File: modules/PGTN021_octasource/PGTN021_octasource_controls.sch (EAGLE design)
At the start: 81 parts

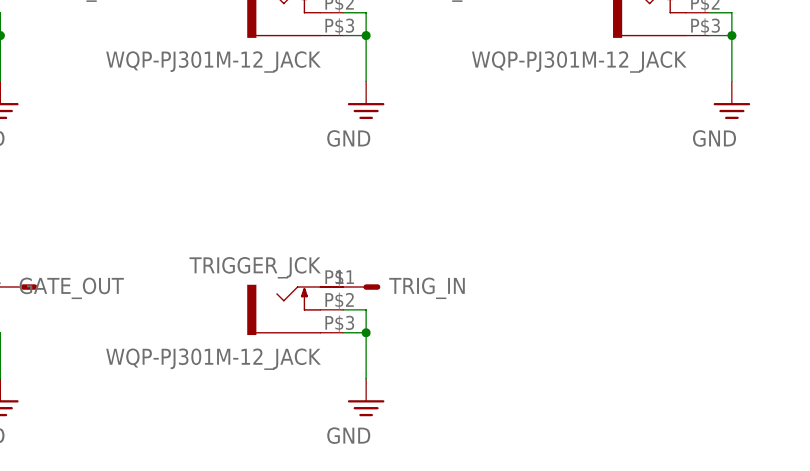
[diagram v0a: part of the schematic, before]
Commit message: Modified boards to fit together better
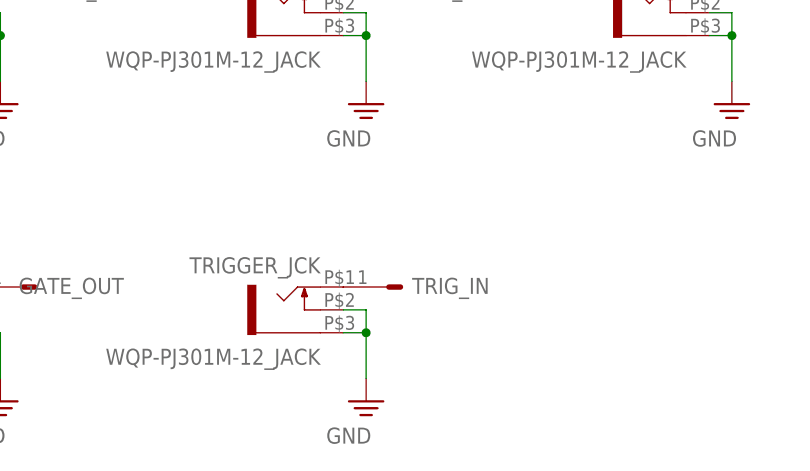
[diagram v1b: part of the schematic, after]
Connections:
- new net N$38: TRIGGER_JCK.2, TRIG_IN.3
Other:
- moved on the sheet: TRIG_IN
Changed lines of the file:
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@@
 <instance part="LENGTH_CV" gate="HEADER" x="45.72" y="-10.16" rot="R180"/>
 <instance part="GATE_OUT" gate="HEADER" x="-35.56" y="-43.18" rot="R180"/>
-<instance part="TRIG_IN" gate="HEADER" x="2.54" y="-43.18" rot="R180"/>
+<instance part="TRIG_IN" gate="HEADER" x="5.08" y="-43.18" rot="R180"/>
 <instance part="SUPPLY15" gate="GND" x="-35.56" y="-55.88"/>
 <instance part="SUPPLY16" gate="GND" x="5.08" y="-55.88"/>
@@
 </segment>
 </net>
+<net name="N$38" class="0">
+<segment>
+<pinref part="TRIGGER_JCK" gate="G$1" pin="2"/>
+<pinref part="TRIG_IN" gate="HEADER" pin="3"/>
+</segment>
+</net>
